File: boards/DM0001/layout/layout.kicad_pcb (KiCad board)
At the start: 6 copper layers, 24.9 x 51.5 mm, 147 parts, among them IC1 TCAN330DCNT, IC2 LDFPVR, IC3 LDFPVR, IC4 L6387ED, IC5 L6387ED, IC6 L6387ED, IC7 STM32G431C8T6, J1 BM05B-SRSS-TB, J2 BM05B-SRSS-TB, J3 SM05B-SRSS-TB, J4 ?, Q1 STL180N6F7, Q2 STL180N6F7, Q3 STL180N6F7, Q4 STL180N6F7, Q5 STL180N6F7, Q6 STL180N6F7, Y1 CSTNE8M00GH5C000R0

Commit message: clean components
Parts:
- C5: value 4.7nF 16V -> 4.7nF 50V X7R
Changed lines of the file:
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@@
 			)
 		)
-		(property "Datasheet" "https://www.jst-mfg.com/product/pdf/eng/eSH.pdf"
-			(at 0 0 0)
-			(layer "F.Fab")
-			(hide yes)
-			(effects
-				(font
-					(size 1.27 1.27)
-					(thickness 0.15)
-				)
-			)
-		)
-		(property "Description" "SM05B-SRSS-TB"
+		(property "Datasheet" "/Users/nasheed/GitHub/demo/components/JST_JAPAN_SOLDERLESS_TERMINALS/SM05B-SRSS-TB/SM05B-SRSS-TB.pdf"
+			(at 0 0 0)
+			(layer "F.Fab")
+			(hide yes)
+			(effects
+				(font
+					(size 1.27 1.27)
+					(thickness 0.15)
+				)
+			)
+		)
+		(property "Description" "Connector Header Surface Mount, Right Angle 5 position 0.039\" (1.00mm)"
 			(at 0 0 0)
 			(layer "F.Fab")
@@
 			)
 		)
-		(property "Value" "4.7nF 16V"
+		(property "Value" "4.7nF 50V X7R"
 			(at 0 1.16 0)
 			(layer "F.Fab")
@@
 			)
 		)
-		(property "Description" "4.7nF 16V"
+		(property "Description" "4.7nF 50V X7R"
 			(at 0 0 180)
 			(unlocked yes)
@@
 			)
 		)
-		(property "Voltage" "16V"
+		(property "Voltage" "50V"
 			(at 0 0 0)
 			(layer "F.SilkS")
@@
 			)
 		)
-		(property "Dielectric" "None"
-			(at 0 0 0)
-			(layer "F.SilkS")
+		(property "Dielectric" "X7R"
+			(at 0 0 0)
+			(layer "F.SilkS")

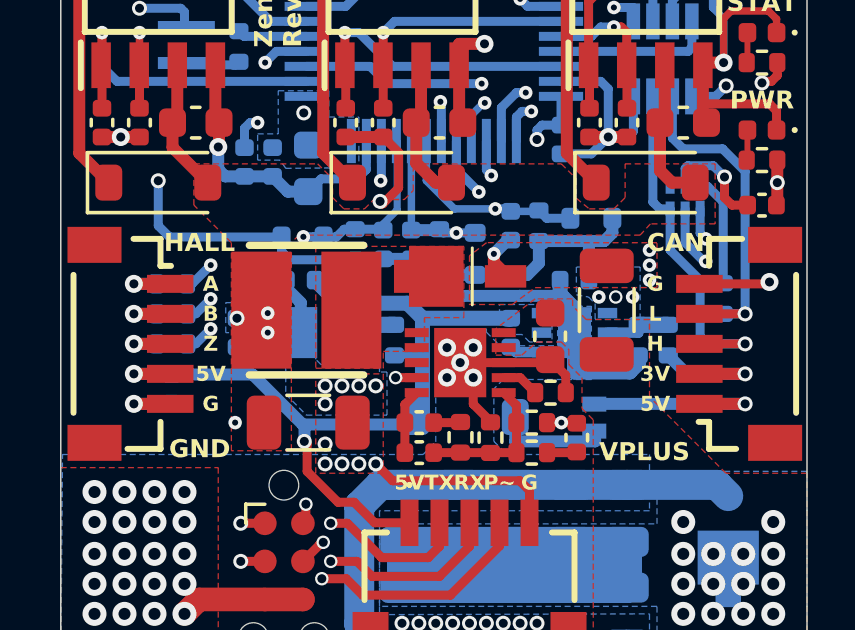
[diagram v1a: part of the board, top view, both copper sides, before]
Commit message: pass drc no unconnected nets + bom matched
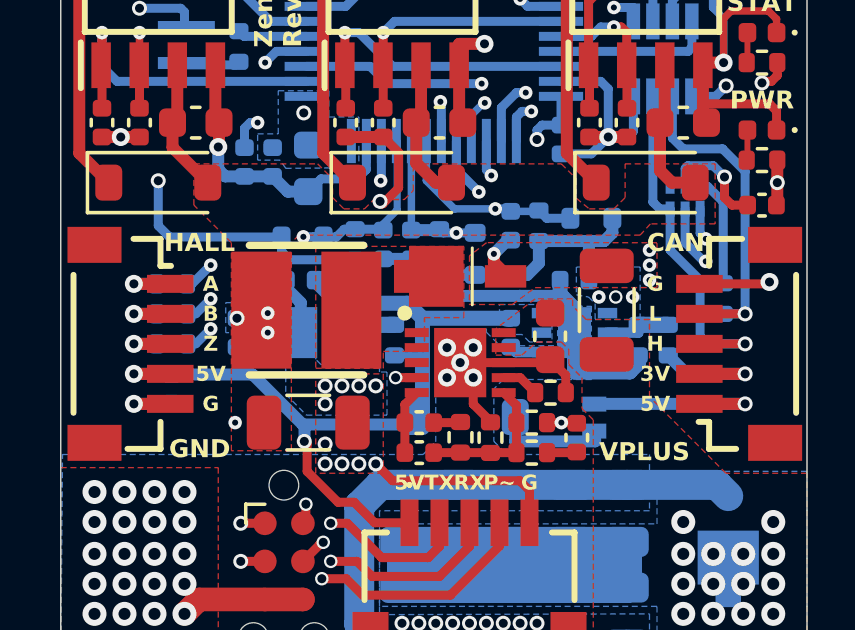
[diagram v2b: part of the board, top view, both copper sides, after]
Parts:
- C1: value 10uF 50V X7R -> CL31B106KAHNNNE
- C15, C17: value 1uF 25V -> CL05A105KP5NNNC
- C16, C18: value 2.2uF 10V -> CL05A225MQ5NNNC
- C19, C24, C29: value 1nF 100V -> GRM1885C1H102JA01D
- C23, C28, C33: value 470nF 16V -> CL10A474KA8NNNC
- C3: value 22uF 25V -> CL31A226MOCLNNC
- C34, C35, C36, C37, C38, C39, C40, C41, C42, C43: value 22uF 35V X5R -> C2012X5R1V226M125AC
- C48: value 1uF 25V X5R -> CL05A105KP5NNNC
- C5: value 4.7nF 50V X7R -> GRM155R71H472KA01D
- C6: value 3.9nF 16V -> CL05B392KB5NNNC
- C7: value 10nF 1% 10V X7R -> CL05B103KB5NNNC
- FB1: value 600 100MHz -> MMZ1005S601CT000
- J1, J2: value BM05B-SRSS-TB -> BM05B-SRSS-TB(LF)(SN)
- J3: value SM05B-SRSS-TB -> SM05B-SRSS-TB(LF)(SN)
- R23, R31, R39: value 1 -> RC0805JR-071RL

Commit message: Sync layouts (#61)
* Sync reference design layouts

* Remove stale properties

* Update board layouts
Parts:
- renumbered C36 to C35, C37 to C36, C38 to C37, C39 to C38, C40 to C39, C41 to C40, C42 to C41, C43 to C42, C35 to C43
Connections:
- net Buck.NC_SYNC renamed Buck.L7986TR.NC_L7986TR_SYNCH
- net Can_Interface.NC_B0 renamed Can_Interface.FSA5157L6X.FSA5157L6X.NC_FSA5157L6X_B0
- net Can_Interface.NC_MP1 renamed Can_Interface.JST_CAN.NC_BM05B-SRSS-TB_MP1
- net Can_Interface.NC_MP2 renamed Can_Interface.JST_CAN.NC_BM05B-SRSS-TB_MP2
- net Ldo_3V3.NC_PG renamed Ldo_3V3.LDFPVR.NC_LDFPVR_PG
- net Ldo_5V.NC_PG renamed Ldo_5V.LDFPVR.NC_LDFPVR_PG
- net NC_PWM_MP1 renamed PwmHeader.NC_SM05B-SRSS-TB_MP1
- net NC_PWM_MP2 renamed PwmHeader.NC_SM05B-SRSS-TB_MP2
- net nRST renamed NRST
